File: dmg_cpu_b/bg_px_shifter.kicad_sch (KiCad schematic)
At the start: 98 parts

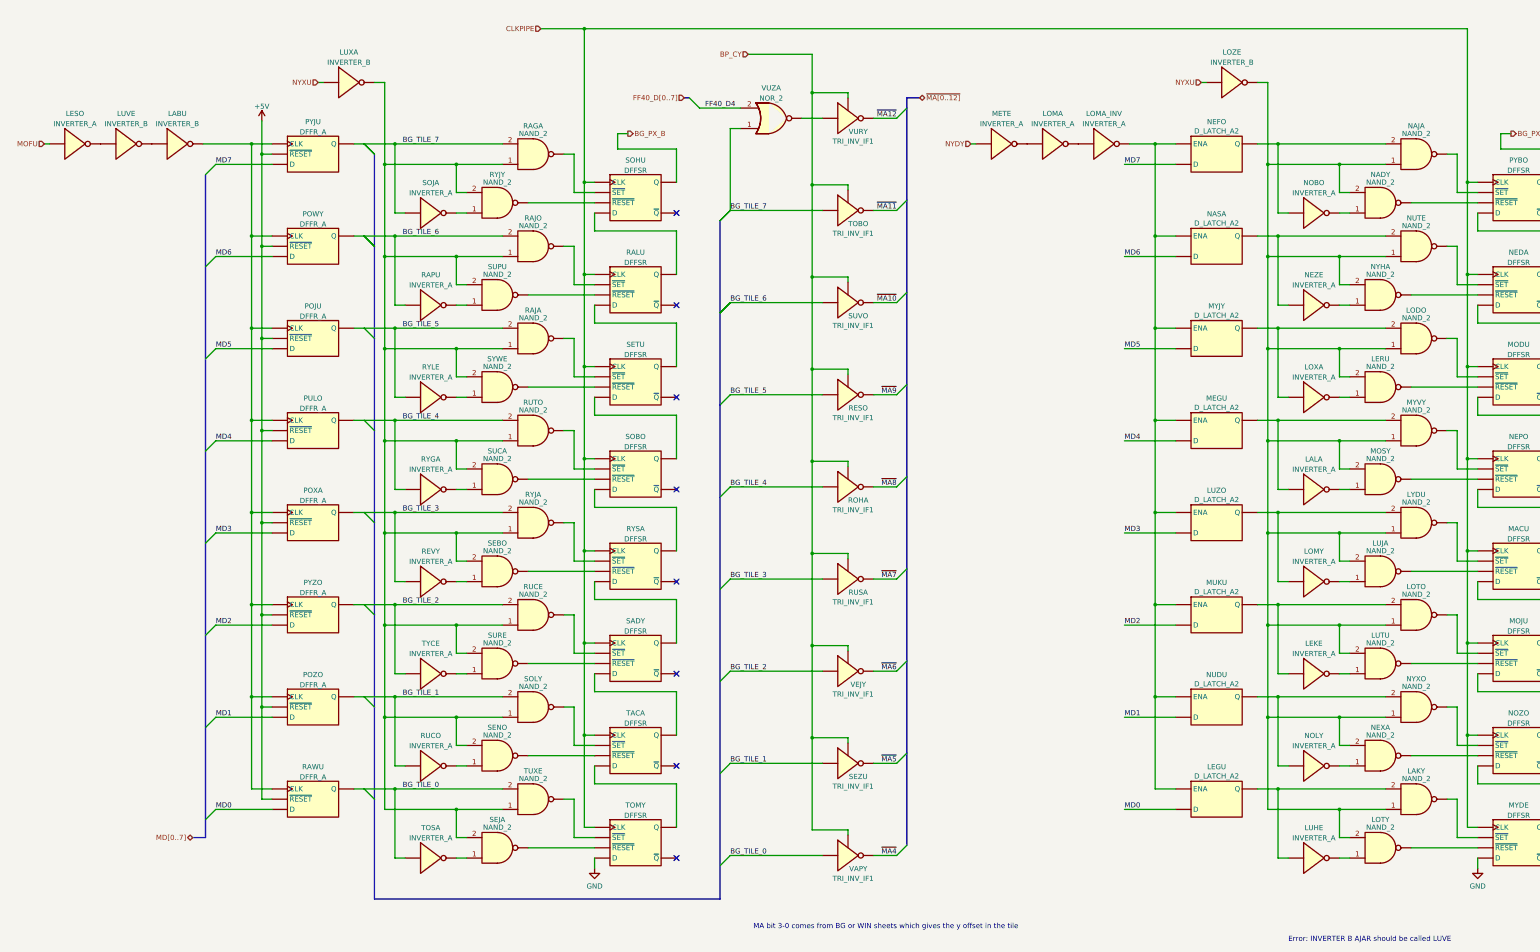
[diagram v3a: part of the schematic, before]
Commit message: PPU hierarchical page progress. Elements moved out of window sheet to be includes in BG and WIN cycles sheet
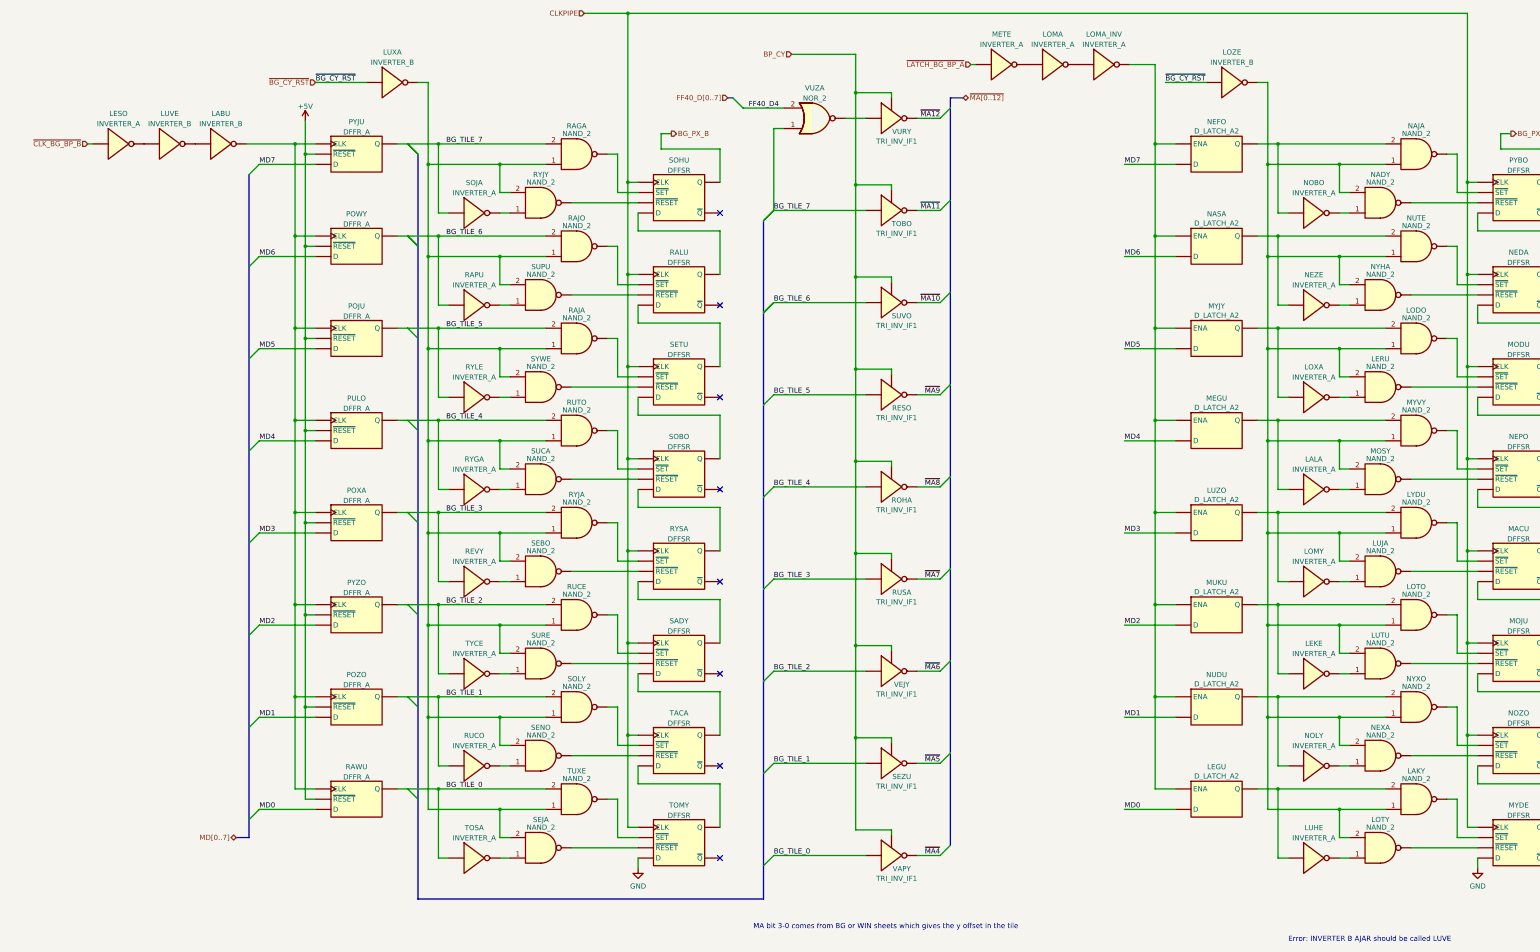
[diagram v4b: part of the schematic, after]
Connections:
- net MOFU renamed ~{CLK_BG_BP_B}
- net NYDY renamed ~{LATCH_BG_BP_A}
- net NYXU renamed ~{BG_CY_RST}
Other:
- moved on the sheet: LABU, LESO, LOMA, LOMA_INV, LUVE, LUXA, METE, POJU, POWY, POXA, POZO, PULO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

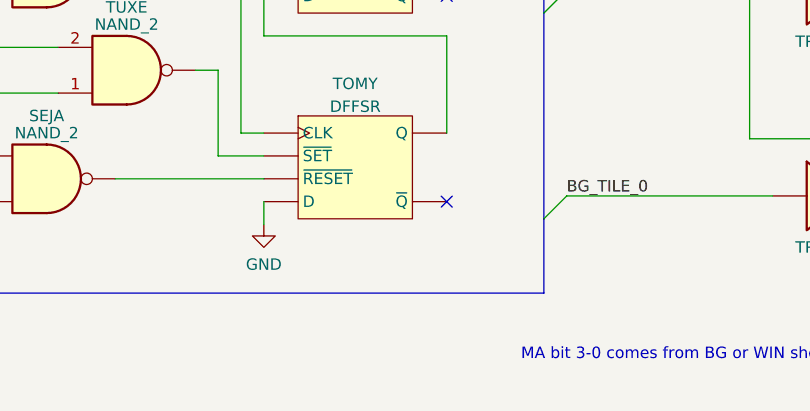
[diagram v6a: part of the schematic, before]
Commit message: Fixed PHI signals.
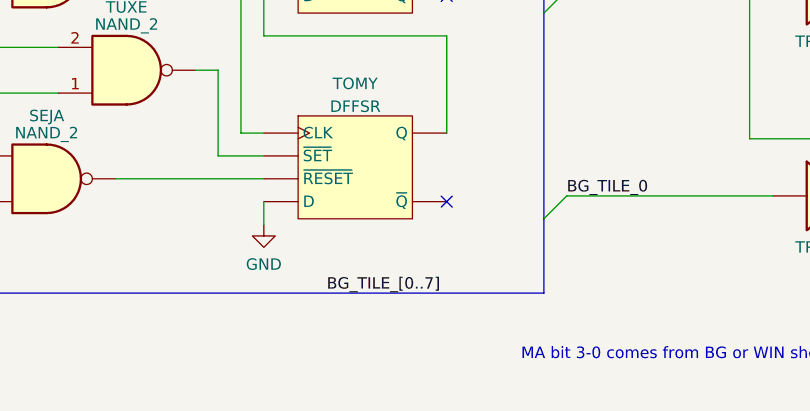
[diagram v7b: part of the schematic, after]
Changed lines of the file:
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@@
     (effects (font (size 1.27 1.27)) (justify right bottom))
+  )
+  (label "BG_TILE_[0..7]" (at 175.26 241.3 0)
+    (effects (font (size 1.27 1.27)) (justify left bottom))
   )
   (label "MD5" (at 74.295 104.775 0)
